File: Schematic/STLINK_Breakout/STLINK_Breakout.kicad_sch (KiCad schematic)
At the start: 12 parts, among them J1 CN11, J2 CN3, J3 CN12, J4 To Nucleo STLINK Adapter, J5 IDC8, J6 FFC8

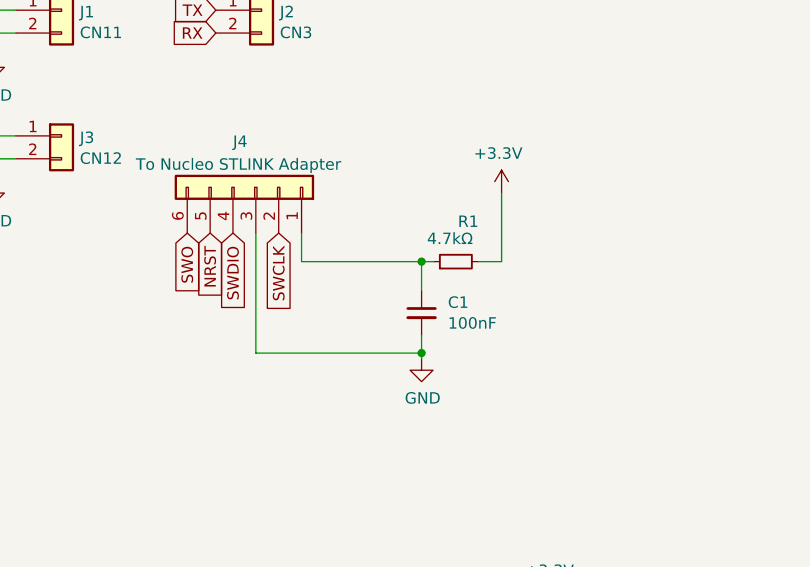
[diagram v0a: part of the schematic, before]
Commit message: Added pull-up resistor for Reset
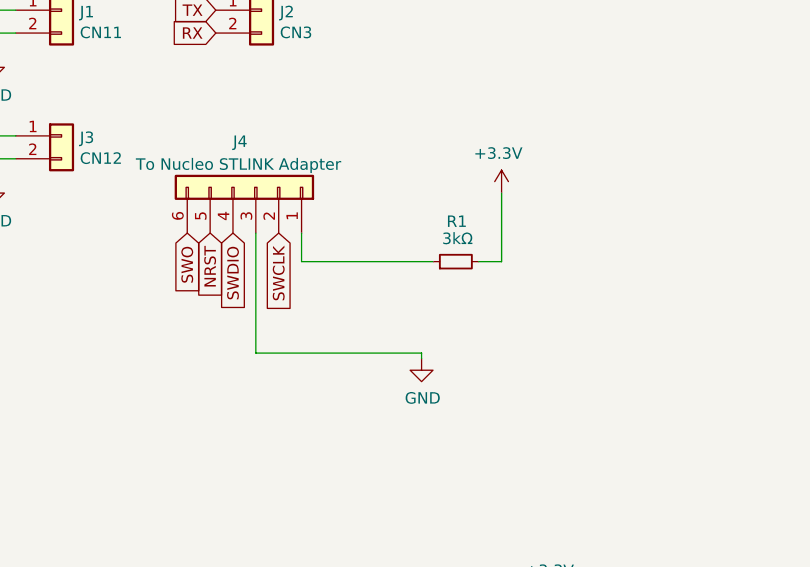
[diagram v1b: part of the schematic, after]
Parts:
- removed C1: 100nF, Capacitor_SMD:C_0603_1608Metric_Pad1.08x0.95mm_HandSolder, symbol Device:C_Small
- R1: value 4.7kΩ -> 3kΩ
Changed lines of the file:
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@@
   (title_block
     (title "ST-Link Breakout")
-    (date "2023-02-01")
+    (date "2023-09-09")
     (company "Retronics - Bjørner Sandom")
   )
@@
   (junction (at 26.035 27.305) (diameter 0) (color 0 0 0 0)
   )
-  (junction (at 73.66 55.245) (diameter 0) (color 0 0 0 0)
-  )
   (junction (at 26.035 29.845) (diameter 0) (color 0 0 0 0)
   )
-  (junction (at 73.66 65.405) (diameter 0) (color 0 0 0 0)
-  )
   (junction (at 26.035 43.815) (diameter 0) (color 0 0 0 0)
   )
@@
     (stroke (width 0) (type default))
   )
-  (wire (pts (xy 73.66 55.245) (xy 73.66 58.42))
-    (stroke (width 0) (type default))
-  )
   (wire (pts (xy 76.2 106.045) (xy 89.535 106.045))
     (stroke (width 0) (type default))
@@
     (stroke (width 0) (type default))
   )
+  (wire (pts (xy 55.245 65.405) (xy 73.66 65.405))
+    (stroke (width 0) (type default))
+  )
   (wire (pts (xy 26.035 27.305) (xy 28.575 27.305))
     (stroke (width 0) (type default))
@@
     (stroke (width 0) (type default))
   )
-  (wire (pts (xy 73.66 55.245) (xy 74.93 55.245))
-    (stroke (width 0) (type default))
-  )
   (wire (pts (xy 29.845 99.06) (xy 35.56 99.06))
     (stroke (width 0) (type default))
   )
-  (wire (pts (xy 55.245 65.405) (xy 73.66 65.405))
-    (stroke (width 0) (type default))
-  )
   (wire (pts (xy 88.265 95.885) (xy 89.535 95.885))
     (stroke (width 0) (type default))
@@
     (stroke (width 0) (type default))
   )
-  (wire (pts (xy 60.325 55.245) (xy 73.66 55.245))
-    (stroke (width 0) (type default))
-  )
   (wire (pts (xy 28.575 29.845) (xy 26.035 29.845))
     (stroke (width 0) (type default))
   )
+  (wire (pts (xy 60.325 55.245) (xy 74.93 55.245))
+    (stroke (width 0) (type default))
+  )
   (wire (pts (xy 26.035 104.14) (xy 35.56 104.14))
     (stroke (width 0) (type default))
   )
   (wire (pts (xy 80.01 55.245) (xy 82.55 55.245))
-    (stroke (width 0) (type default))
-  )
-  (wire (pts (xy 73.66 63.5) (xy 73.66 65.405))
     (stroke (width 0) (type default))
   )
@@
     )
   )
-  (symbol (lib_id "Device:C_Small") (at 73.66 60.96 0) (unit 1)
-    (in_bom yes) (on_board yes) (dnp no)
-    (property "Reference" "C1" (at 76.581 59.7916 0)
-      (effects (font (size 1.27 1.27)) (justify left))
-    )
-    (property "Value" "100nF" (at 76.581 62.103 0)
-      (effects (font (size 1.27 1.27)) (justify left))
-    )
-    (property "Footprint" "Capacitor_SMD:C_0603_1608Metric_Pad1.08x0.95mm_HandSolder" (at 73.66 60.96 0)
-      (effects (font (size 1.27 1.27)) hide)
-    )
-    (property "Datasheet" "~" (at 73.66 60.96 0)
-      (effects (font (size 1.27 1.27)) hide)
-    )
-    (pin "1")
-    (pin "2")
-    (instances
-      (project "STLINK_Breakout"
-        (path "/87df3795-a0c9-46c2-a391-09ea3c6d9908"
-          (reference "C1") (unit 1)
-        )
-      )
-    )
-  )
   (symbol (lib_id "power:+3.3V") (at 29.845 95.25 0) (unit 1)
     (in_bom yes) (on_board yes) (dnp no)
@@
   (symbol (lib_id "Device:R_Small") (at 77.47 55.245 90) (unit 1)
     (in_bom yes) (on_board yes) (dnp no)
-    (property "Reference" "R1" (at 80.01 50.8 90)
-      (effects (font (size 1.27 1.27)) (justify left))
-    )
-    (property "Value" "4.7kΩ" (at 79.375 52.705 90)
-      (effects (font (size 1.27 1.27)) (justify left))
-    )
+    (property "Reference" "R1" (at 78.74 50.8 90)
+      (effects (font (size 1.27 1.27)) (justify left))
+    )
+    (property "Value" "3kΩ" (at 79.375 52.705 90)
+      (effects (font (size 1.27 1.27)) (justify left))
+    )

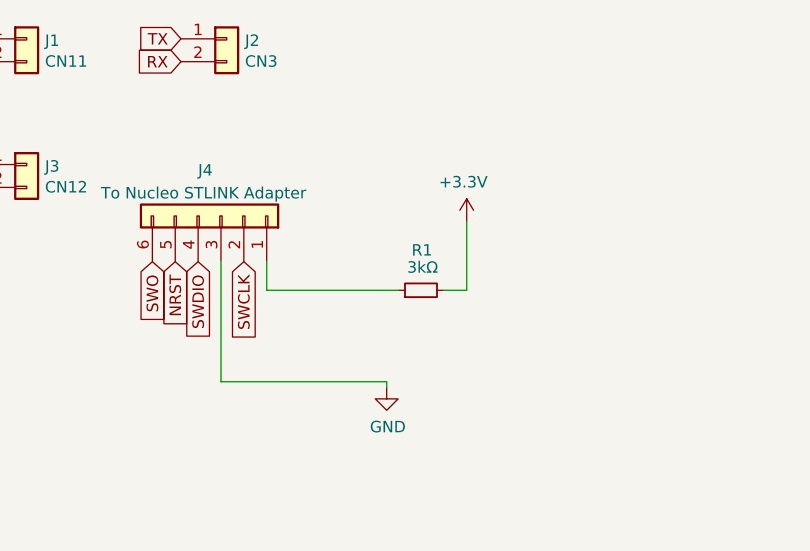
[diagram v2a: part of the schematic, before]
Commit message: Changed resistor value
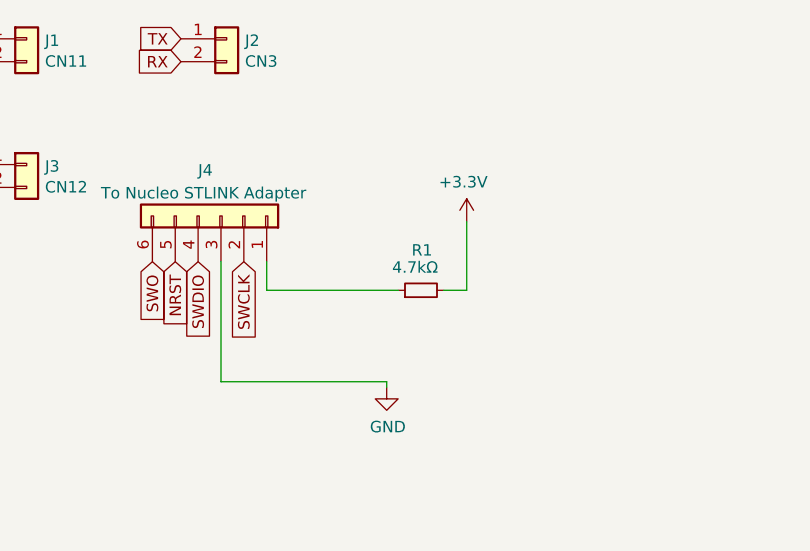
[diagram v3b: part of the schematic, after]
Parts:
- R1: value 3kΩ -> 4.7kΩ
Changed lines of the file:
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@@
       (effects (font (size 1.27 1.27)) (justify left))
     )
-    (property "Value" "3kΩ" (at 79.375 52.705 90)
+    (property "Value" "4.7kΩ" (at 79.375 52.705 90)
       (effects (font (size 1.27 1.27)) (justify left))
     )

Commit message: Added ESD protection for USB.
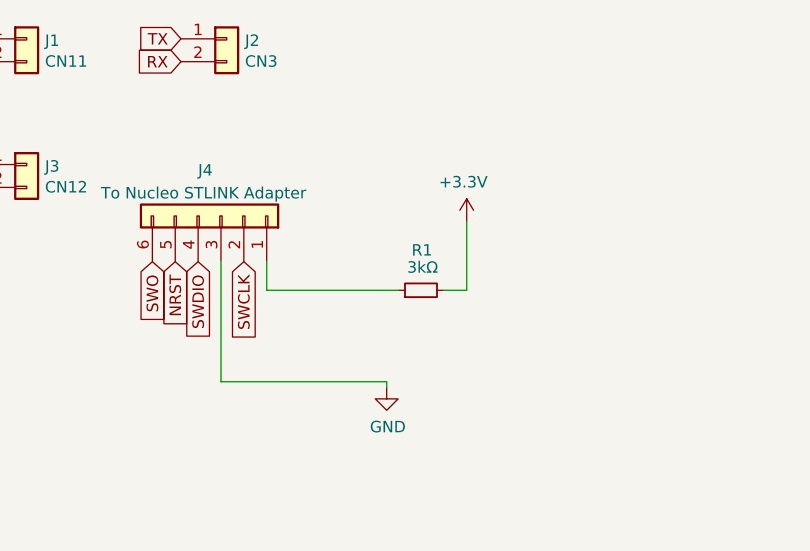
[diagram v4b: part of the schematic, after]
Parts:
- R1: value 4.7kΩ -> 3kΩ
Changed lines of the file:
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@@
       (effects (font (size 1.27 1.27)) (justify left))
     )
-    (property "Value" "4.7kΩ" (at 79.375 52.705 90)
+    (property "Value" "3kΩ" (at 79.375 52.705 90)
       (effects (font (size 1.27 1.27)) (justify left))
     )
